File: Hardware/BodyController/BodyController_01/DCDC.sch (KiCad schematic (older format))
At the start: 54 parts, among them Q12 BUK7J1R4-40HX, Q13 BUK7J1R4-40HX, Q16 2N7002, Q6 NX1029X,115, Q7 NX1029X,115, U21 LM2903QDRQ1, U25 UCC27511A-Q1, U27 INA21x

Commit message: New bring-up code for Body Controller
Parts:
- C70, C76, C77, C78, C80, C81: MPN CGA4J3X7R1H105K125AE -> CGA4J3X7R1H105M125AE
- C71: value 2u2 -> 4u7; MPN CGA5L3X7R1H225M160AE -> CGA5L3X7R1H475K160AE
- D21, D23: MPN MMSZ4702T1G -> MMSZ5245BT1G
- R142: value 1R0 -> 3R0; MPN AC0603JR-071RL -> ERJ-3GEYJ3R0V
- R148, R149, R150, R154, R155: value 10R -> 3R0; MPN AC0603FR-0710RL -> ERJ-3GEYJ3R0V
- R160: value 1k -> 4k7; MPN AC0603FR-071KL -> AC0603FR-074K7L
- U21: MPN LM2903QDRQ1 -> LM2903AVQPWRG4Q1

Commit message: too much work to specify all. New Scheduler, new bootloader, added new Hardware projects, updated code for bringup, COnverted kicad files to new version.
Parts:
- C57, C69, C70, C71, C72, C73, C74, C75, C76, C77, C78, C80, C81: symbol C -> BodyController_01-rescue:C-RESCUE-BodyController_01
- D16: symbol D_Schottky_x2_Serial_AKC -> BodyController_01-rescue:D_Schottky_x2_Serial_AKC-RESCUE-BodyController_01
- D21, D23: symbol D_Zener -> BodyController_01-rescue:D_Zener-RESCUE-BodyController_01
- D25: symbol D -> BodyController_01-rescue:D-RESCUE-BodyController_01
- D26, D27: symbol D_Schottky -> BodyController_01-rescue:D_Schottky-RESCUE-BodyController_01
- NT3, NT4: symbol Net_Tie-0.5mm -> BodyController_01-rescue:Net_Tie-0.5mm-RESCUE-BodyController_01
- Q12, Q13: symbol BUK9Y3R0-40E,115 -> BodyController_01-rescue:BUK9Y3R0-40E,115-RESCUE-BodyController_01
- Q16: symbol Q_NMOS_GSD -> BodyController_01-rescue:Q_NMOS_GSD-RESCUE-BodyController_01
- Q6, Q7: symbol NX1029X,115 -> BodyController_01-rescue:NX1029X,115-RESCUE-BodyController_01
- R133, R134, R135, R136, R137, R138, R139, R140, R141, R142, R143, R144, R145, R146, R147, R148, R149, R150, R152, R153, R154, R155, R156, R160, R162: symbol R -> BodyController_01-rescue:R-RESCUE-BodyController_01
- U21: symbol LM2903QDRQ1 -> BodyController_01-rescue:LM2903QDRQ1-RESCUE-BodyController_01
- U25: symbol UCC27511A-Q1 -> BodyController_01-rescue:UCC27511A-Q1-RESCUE-BodyController_01
- U27: symbol INA21x -> BodyController_01-rescue:INA21x-RESCUE-BodyController_01

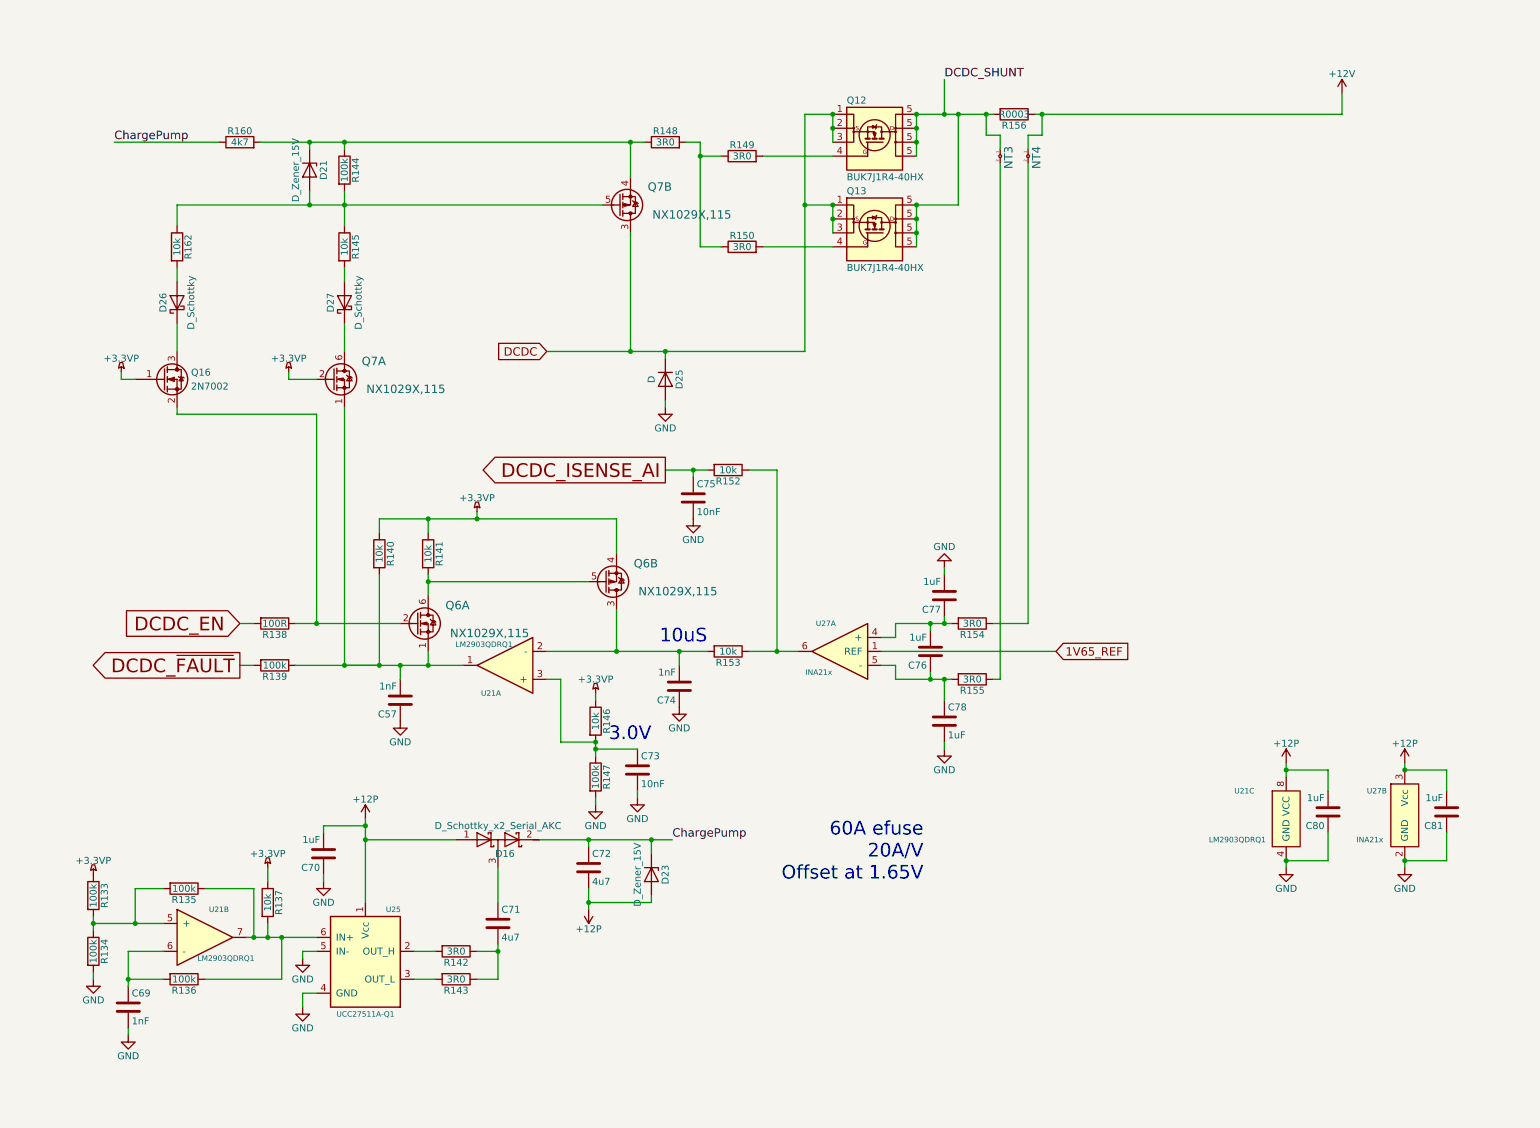
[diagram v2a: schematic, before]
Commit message: BMS controller. Lots of new FW including bootloaders
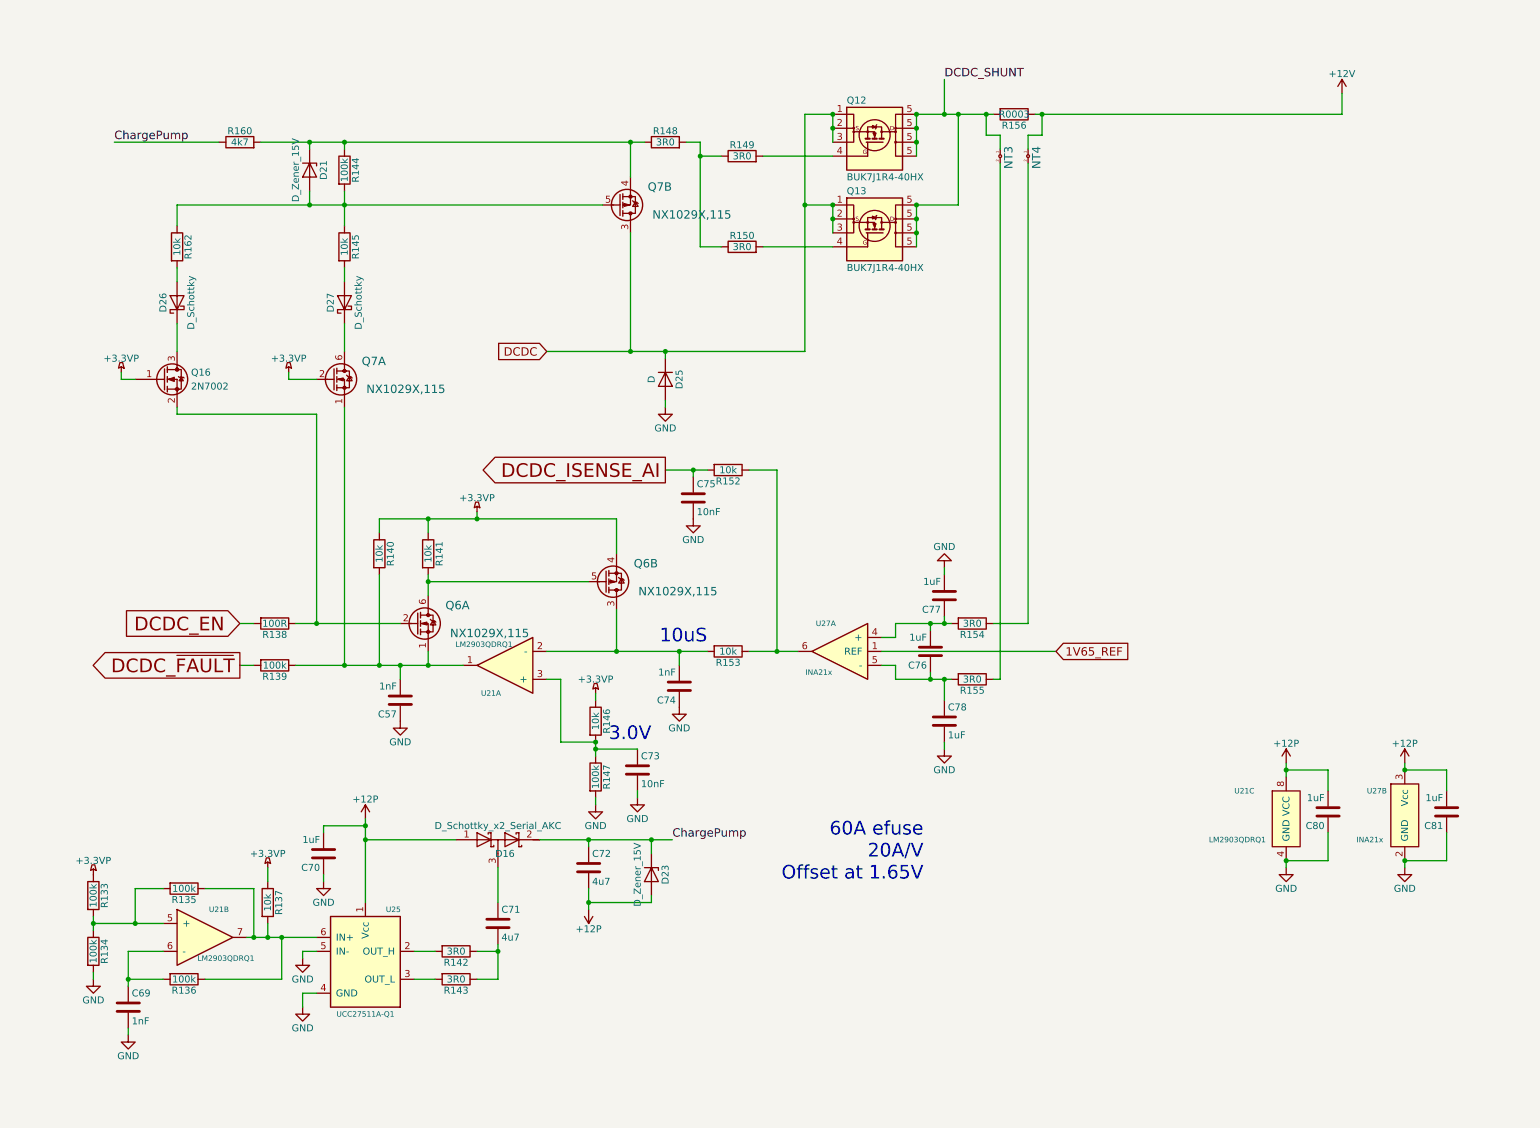
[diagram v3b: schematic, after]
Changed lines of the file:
@@
 1V65_REF
 Wire Wire Line
-	7300 900  9500 900
-Wire Wire Line
-	1750 1100 4500 1100
+	7300 900  7350 900
+Wire Wire Line
+	1750 1100 2100 1100
 Wire Wire Line
 	4800 1100 4900 1100
@@
 	7000 4550 7250 4550
 Wire Wire Line
-	6300 4550 6700 4550
-Wire Wire Line
-	6300 4950 6700 4950
+	6300 4550 6550 4550
+Wire Wire Line
+	6300 4950 6550 4950
 Wire Wire Line
 	7000 4950 7050 4950
@@
 	5450 3450 5250 3450
 Wire Wire Line
-	4650 3450 4950 3450
+	4650 3450 4850 3450
 Wire Wire Line
 	4850 3450 4850 3500
 Wire Wire Line
-	5250 4750 5600 4750
-Wire Wire Line
-	3800 4750 4950 4750
+	5250 4750 5450 4750
+Wire Wire Line
+	3800 4750 4300 4750
 Wire Wire Line
 	4750 4850 4750 4750
@@
 	4150 5850 4150 5800
 Wire Wire Line
-	4150 5400 4150 5500
+	4150 5400 4150 5450
 Wire Wire Line
 	4150 5100 4150 5050
@@
 	9400 5600 9400 5750
 Wire Wire Line
-	2000 4850 3200 4850
+	2000 4850 2350 4850
 Wire Wire Line
 	2950 4750 2950 4850
@@
 	10250 6250 10250 6050
 Wire Wire Line
-	2950 4200 2950 4350
+	2950 4200 2950 4250
 Wire Wire Line
 	2950 4250 4100 4250
@@
 	4300 3800 4300 4050
 Wire Wire Line
-	2600 3800 4300 3800
+	2600 3800 2950 3800
 Wire Wire Line
 	2950 3900 2950 3800
@@
 	3900 4950 3800 4950
 Wire Wire Line
-	9100 5550 9100 5650
+	9100 5550 9100 5600
 Wire Wire Line
 	9100 5600 9400 5600
@@
 	9400 6250 9400 6050
 Wire Wire Line
-	2000 4550 2750 4550
+	2000 4550 2150 4550
 Wire Wire Line
 	4400 1100 4400 1350
@@
 	2350 1100 2350 1150
 Wire Wire Line
-	2350 1450 2350 1700
-Wire Wire Line
-	1150 1550 4200 1550
+	2350 1450 2350 1550
+Wire Wire Line
+	1150 1550 2100 1550
 Wire Wire Line
 	1950 2800 2150 2800
@@
 	1700 4850 1600 4850
 Wire Wire Line
-	2500 5950 2500 6550
+	2500 5950 2500 6000
 Wire Wire Line
 	2500 6000 2200 6000
@@
 	2200 6400 2200 6350
 Wire Wire Line
-	4100 6450 4100 6600
+	4100 6450 4100 6550
 Wire Wire Line
 	4100 6150 4100 6100
 Wire Wire Line
-	3750 6100 4700 6100
+	3750 6100 4100 6100
 Wire Wire Line
 	2150 6900 2050 6900
@@
 	2050 7200 2150 7200
 Wire Wire Line
-	3450 6850 3450 7100
+	3450 6850 3450 6900
 Wire Wire Line
 	2050 6900 2050 6950
@@
 	2050 7200 2050 7300
 Wire Wire Line
-	1650 6800 2150 6800
+	1650 6800 1700 6800
 Wire Wire Line
 	1800 6300 1800 6400
@@
 	1800 6700 1800 6800
 Wire Wire Line
-	550  6700 1050 6700
+	550  6700 850  6700
 Wire Wire Line
 	1700 6800 1700 6450
@@
 	550  7100 550  7050
 Wire Wire Line
-	550  6650 550  6750
+	550  6650 550  6700
 Wire Wire Line
 	1050 6450 850  6450
@@
 	1050 7100 800  7100
 Wire Wire Line
-	800  6900 800  7150
+	800  6900 800  7100
 Wire Wire Line
 	3450 6900 3300 6900
@@
 	4550 6100 4550 6200
 Wire Wire Line
-	5650 2600 3800 2600
+	5650 2600 4650 2600
 Wire Wire Line
 	9500 900  9500 750
@@
 	3450 6300 3450 6550
 Wire Wire Line
-	5650 900  5650 2600
+	5650 900  5650 1550
 Wire Wire Line
 	5650 900  5850 900
 Wire Wire Line
-	5850 900  5850 1100
+	5850 900  5850 1000
 Wire Wire Line
 	5650 1550 5850 1550
 Wire Wire Line
-	5850 1550 5850 1750
+	5850 1550 5850 1650
 Wire Wire Line
 	5050 1200 4900 1200
@@
 	6750 900  6750 1550
 Wire Wire Line
-	6450 1550 6450 1850
+	6450 1550 6450 1650
 Wire Wire Line
 	6750 1550 6450 1550
 Wire Wire Line
-	6450 900  6450 1200
+	6450 900  6450 1000
 Wire Wire Line
 	1150 1700 1150 1550
@@
 	2750 4950 2750 4850
 Wire Wire Line
-	4900 1100 4900 1850
+	4900 1100 4900 1200
 Wire Wire Line
 	7050 1050 6950 1050
@@
 	6650 650  6650 900
 Wire Wire Line
-	6450 900  7000 900
+	6450 900  6650 900
 Wire Wire Line
 	6200 4750 7450 4750
@@
 Connection ~ 7350 900
 Connection ~ 6650 900
+Wire Wire Line
+	6650 4550 6700 4550
+Wire Wire Line
+	6650 4950 6700 4950
+Wire Wire Line
+	6550 4550 6650 4550
+Wire Wire Line
+	6550 4950 6650 4950
+Wire Wire Line
+	5450 4750 5600 4750
+Wire Wire Line
+	4850 3450 4950 3450
+Wire Wire Line
+	4750 4750 4950 4750
+Wire Wire Line
+	4150 5450 4150 5500
+Wire Wire Line
+	4300 4750 4750 4750
+Wire Wire Line
+	2950 4250 2950 4350
+Wire Wire Line
+	2950 3800 3300 3800
+Wire Wire Line
+	3300 3800 4300 3800
+Wire Wire Line
+	2950 4850 3200 4850
+Wire Wire Line
+	9100 5600 9100 5650
+Wire Wire Line
+	4400 1100 4500 1100
+Wire Wire Line
+	4400 2600 3800 2600
+Wire Wire Line
+	2350 1550 2350 1700
+Wire Wire Line
+	2350 1550 4200 1550
+Wire Wire Line
+	2600 4850 2750 4850
+Wire Wire Line
+	2500 6000 2500 6100
+Wire Wire Line
+	2500 6100 2500 6550
+Wire Wire Line
+	3450 6900 3450 7100
+Wire Wire Line
+	1800 6800 1900 6800
+Wire Wire Line
+	1700 6800 1800 6800
+Wire Wire Line
+	1900 6800 2150 6800
+Wire Wire Line
+	550  6700 550  6750
+Wire Wire Line
+	850  6700 1050 6700
+Wire Wire Line
+	800  7100 800  7150
+Wire Wire Line
+	2350 1100 4400 1100
+Wire Wire Line
+	4100 6550 4100 6600
+Wire Wire Line
+	4100 6100 4550 6100
+Wire Wire Line
+	4550 6100 4700 6100
+Wire Wire Line
+	2100 1100 2350 1100
+Wire Wire Line
+	4650 2600 4400 2600
+Wire Wire Line
+	5850 1000 5850 1100
+Wire Wire Line
+	5650 1550 5650 2600
+Wire Wire Line
+	5850 1650 5850 1750
+Wire Wire Line
+	4900 1200 4900 1850
+Wire Wire Line
+	6750 900  6950 900
+Wire Wire Line
+	6450 1000 6450 1100
+Wire Wire Line
+	6450 1100 6450 1200
+Wire Wire Line
+	6450 1650 6450 1750
+Wire Wire Line
+	6450 1750 6450 1850
+Wire Wire Line
+	2100 1550 2350 1550
+Wire Wire Line
+	2150 4550 2750 4550
+Wire Wire Line
+	2750 4850 2950 4850
+Wire Wire Line
+	6950 900  7000 900
+Wire Wire Line
+	7350 900  9500 900
+Wire Wire Line
+	6650 900  6750 900
 $EndSCHEMATC
